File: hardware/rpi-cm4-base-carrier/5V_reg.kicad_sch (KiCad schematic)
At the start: 10 parts, among them IC5 LMR51450FNDRRR

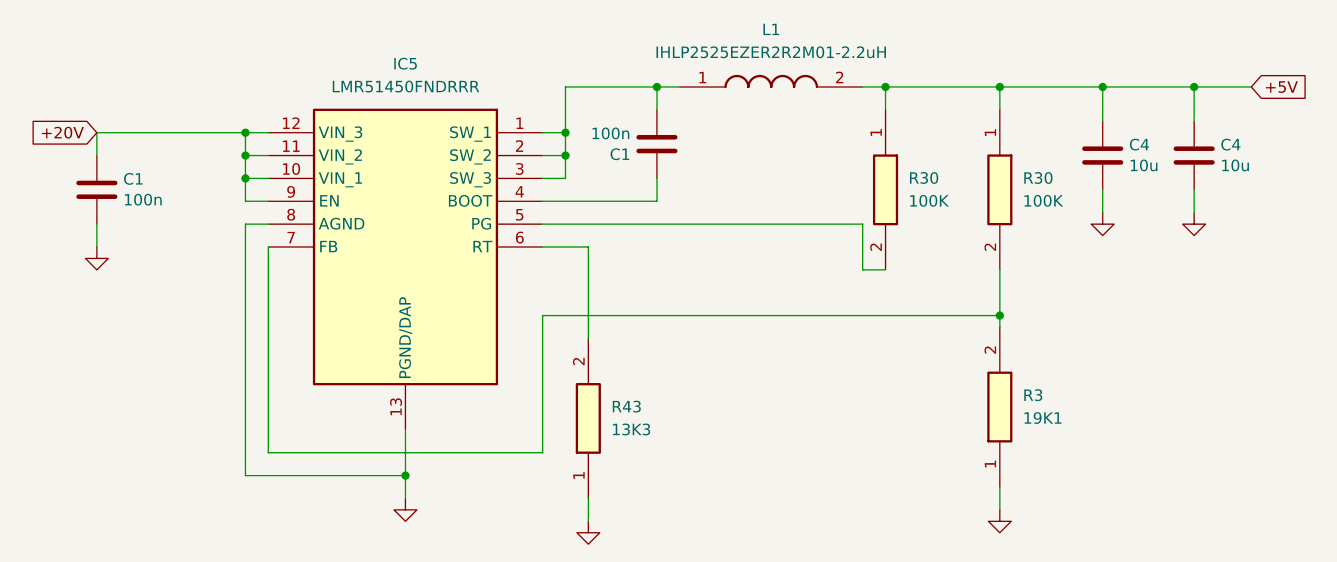
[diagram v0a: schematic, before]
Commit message: convert IC refs to U refs and re-annotate, add fiducials and extra via stitching to layout
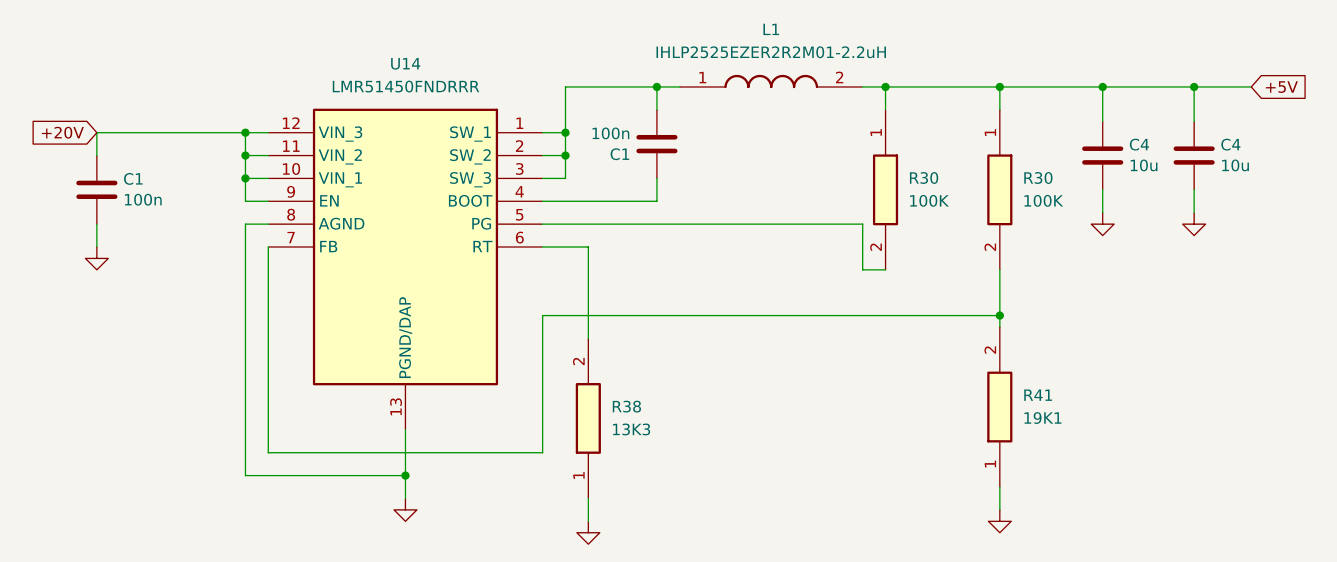
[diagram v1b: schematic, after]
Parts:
- renumbered R43 to R38, R3 to R41, IC5 to U14
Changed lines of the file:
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@@
         )
         (path "/92c58705-ecb0-498b-b561-44a3f0daad57/93ba1a48-bd63-468c-a3b4-483edb456fef/00e84fbb-dda2-4689-a88f-629944c1a860"
-          (reference "#PWR085") (unit 1)
+          (reference "#PWR088") (unit 1)
         )
       )
@@
         )
         (path "/92c58705-ecb0-498b-b561-44a3f0daad57/93ba1a48-bd63-468c-a3b4-483edb456fef/00e84fbb-dda2-4689-a88f-629944c1a860"
-          (reference "#PWR013") (unit 1)
+          (reference "#PWR086") (unit 1)
         )
       )
@@
         )
         (path "/92c58705-ecb0-498b-b561-44a3f0daad57/93ba1a48-bd63-468c-a3b4-483edb456fef/00e84fbb-dda2-4689-a88f-629944c1a860"
-          (reference "#PWR087") (unit 1)
+          (reference "#PWR091") (unit 1)
         )
       )
@@
         )
         (path "/92c58705-ecb0-498b-b561-44a3f0daad57/93ba1a48-bd63-468c-a3b4-483edb456fef/00e84fbb-dda2-4689-a88f-629944c1a860"
-          (reference "#PWR081") (unit 1)
+          (reference "#PWR089") (unit 1)
         )
       )
@@
         )
         (path "/92c58705-ecb0-498b-b561-44a3f0daad57/93ba1a48-bd63-468c-a3b4-483edb456fef/00e84fbb-dda2-4689-a88f-629944c1a860"
-          (reference "R42") (unit 1)
+          (reference "R39") (unit 1)
         )
       )
@@
         )
         (path "/92c58705-ecb0-498b-b561-44a3f0daad57/93ba1a48-bd63-468c-a3b4-483edb456fef/00e84fbb-dda2-4689-a88f-629944c1a860"
-          (reference "#PWR079") (unit 1)
+          (reference "#PWR087") (unit 1)
         )
       )
@@
   (symbol (lib_id "SamacSys_Parts:CR0402-FX-1332GLF") (at 114.3 86.36 90) (unit 1)
     (in_bom yes) (on_board yes) (dnp no) (fields_autoplaced)
-    (property "Reference" "R43" (at 116.84 76.2 90)
+    (property "Reference" "R38" (at 116.84 76.2 90)
       (effects (font (size 1.27 1.27)) (justify right))
     )
@@
       (project "rpi-cm4-base-carrier"
         (path "/92c58705-ecb0-498b-b561-44a3f0daad57/93ba1a48-bd63-468c-a3b4-483edb456fef/00e84fbb-dda2-4689-a88f-629944c1a860"
-          (reference "R43") (unit 1)
+          (reference "R38") (unit 1)
         )
       )
@@
         )
         (path "/92c58705-ecb0-498b-b561-44a3f0daad57/93ba1a48-bd63-468c-a3b4-483edb456fef/00e84fbb-dda2-4689-a88f-629944c1a860"
-          (reference "#PWR086") (unit 1)
+          (reference "#PWR090") (unit 1)
         )
       )
@@
   (symbol (lib_id "SamacSys_Parts:LMR51450FNDRRR") (at 109.22 45.72 0) (mirror y) (unit 1)
     (in_bom yes) (on_board yes) (dnp no)
-    (property "Reference" "IC5" (at 93.98 38.1 0)
+    (property "Reference" "U14" (at 93.98 38.1 0)
       (effects (font (size 1.27 1.27)))
     )
@@
       (project "rpi-cm4-base-carrier"
         (path "/92c58705-ecb0-498b-b561-44a3f0daad57/93ba1a48-bd63-468c-a3b4-483edb456fef/00e84fbb-dda2-4689-a88f-629944c1a860"
-          (reference "IC5") (unit 1)
+          (reference "U14") (unit 1)
         )
       )
@@
   (symbol (lib_id "SamacSys_Parts:CR0402-FX-1912GLF") (at 160.02 85.09 90) (unit 1)
     (in_bom yes) (on_board yes) (dnp no) (fields_autoplaced)
-    (property "Reference" "R3" (at 162.56 74.93 90)
+    (property "Reference" "R41" (at 162.56 74.93 90)
       (effects (font (size 1.27 1.27)) (justify right))
     )
@@
       (project "rpi-cm4-base-carrier"
         (path "/92c58705-ecb0-498b-b561-44a3f0daad57/93ba1a48-bd63-468c-a3b4-483edb456fef/00e84fbb-dda2-4689-a88f-629944c1a860"
-          (reference "R3") (unit 1)
+          (reference "R41") (unit 1)
         )
       )
@@
         )
         (path "/92c58705-ecb0-498b-b561-44a3f0daad57/93ba1a48-bd63-468c-a3b4-483edb456fef/00e84fbb-dda2-4689-a88f-629944c1a860"
-          (reference "R1") (unit 1)
-        )
-      )
+          (reference "R40") (unit 1)
+        )
+      )

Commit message: design files exported ready for manufacture, LCSC part numbers added throughout the library
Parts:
- C1: LCSC Part # (none) -> C152724; LCSC Part Number (none) -> C152724
- C4: LCSC Part # (none) -> C326595; LCSC Part Number (none) -> C326595
- L1: LCSC Part # (none) -> C845037; LCSC Part Number (none) -> C845037
- R30: LCSC Part # (none) -> C131362; LCSC Part Number (none) -> C131362
- R38: LCSC Part # (none) -> C274352; LCSC Part Number (none) -> C274352
- R41: LCSC Part # (none) -> C850847; LCSC Part Number (none) -> C850847
- U14: LCSC Part # (none) -> C6890985; LCSC Part Number (none) -> C6890985
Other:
- title: (none) -> Raspberry Pi Compute Module 4 Control Node
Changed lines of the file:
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@@
 (kicad_sch (version 20230121) (generator eeschema)
   (paper "A4")
+  (title_block
+    (title "Raspberry Pi Compute Module 4 Control Node")
+    (date "2024-02-04")
+    (comment 2 "creativecommons.org/licenses/by-sa/4.0/")
+    (comment 3 "License: CC BY-SA 4.0")
+    (comment 4 "Author: Sam Earnshaw")
+  )
   (junction (at 111.76 45.72) (diameter 0) (color 0 0 0 0)
   )
@@
       (effects (font (size 1.27 1.27)) hide)
     )
+    (property "LCSC Part Number" "C152724" (at 59.69 52.07 0)
+      (effects (font (size 1.27 1.27)) hide)
+    )
+    (property "LCSC Part #" "C152724" (at 59.69 52.07 0)
+      (effects (font (size 1.27 1.27)) hide)
+    )
     (pin "1")
     (pin "2")
@@
       (effects (font (size 1.27 1.27)) hide)
     )
+    (property "LCSC Part Number" "C152724" (at 121.92 46.99 0)
+      (effects (font (size 1.27 1.27)) hide)
+    )
+    (property "LCSC Part #" "C152724" (at 121.92 46.99 0)
+      (effects (font (size 1.27 1.27)) hide)
+    )
     (pin "1")
     (pin "2")
@@
     (property "Manufacturer_Part_Number" "CR0402-FX-1003GLF" (at -648.87 57.15 0)
       (effects (font (size 1.27 1.27)) (justify left top) hide)
+    )
+    (property "LCSC Part Number" "C131362" (at 147.32 43.18 0)
+      (effects (font (size 1.27 1.27)) hide)
+    )
+    (property "LCSC Part #" "C131362" (at 147.32 43.18 0)
+      (effects (font (size 1.27 1.27)) hide)
     )
     (pin "2")
@@
       (effects (font (size 1.27 1.27)) (justify left top) hide)
     )
+    (property "LCSC Part Number" "C845037" (at 124.46 40.64 0)
+      (effects (font (size 1.27 1.27)) hide)
+    )
+    (property "LCSC Part #" "C845037" (at 124.46 40.64 0)
+      (effects (font (size 1.27 1.27)) hide)
+    )
     (pin "2")
     (pin "1")
@@
     )
     (property "Field8" "111893011" (at 181.61 48.26 0)
+      (effects (font (size 1.27 1.27)) hide)
+    )
+    (property "LCSC Part Number" "C326595" (at 181.61 48.26 0)
+      (effects (font (size 1.27 1.27)) hide)
+    )
+    (property "LCSC Part #" "C326595" (at 181.61 48.26 0)
       (effects (font (size 1.27 1.27)) hide)
     )
@@
       (effects (font (size 1.27 1.27)) (justify left top) hide)
     )
+    (property "LCSC Part Number" "C274352" (at 114.3 86.36 0)
+      (effects (font (size 1.27 1.27)) hide)
+    )
+    (property "LCSC Part #" "C274352" (at 114.3 86.36 0)
+      (effects (font (size 1.27 1.27)) hide)
+    )
     (pin "1")
     (pin "2")
@@
     )
     (property "Field8" "111893011" (at 171.45 48.26 0)
+      (effects (font (size 1.27 1.27)) hide)
+    )
+    (property "LCSC Part Number" "C326595" (at 171.45 48.26 0)
+      (effects (font (size 1.27 1.27)) hide)
+    )
+    (property "LCSC Part #" "C326595" (at 171.45 48.26 0)
       (effects (font (size 1.27 1.27)) hide)
     )
@@
     (property "Manufacturer_Part_Number" "LMR51450FNDRRR" (at 82.55 840.64 0)
       (effects (font (size 1.27 1.27)) (justify left top) hide)
+    )
+    (property "LCSC Part Number" "C6890985" (at 109.22 45.72 0)
+      (effects (font (size 1.27 1.27)) hide)
+    )
+    (property "LCSC Part #" "C6890985" (at 109.22 45.72 0)
+      (effects (font (size 1.27 1.27)) hide)
     )
     (pin "13")
@@
       (effects (font (size 1.27 1.27)) (justify left top) hide)
     )
+    (property "LCSC Part Number" "C850847" (at 160.02 85.09 0)
+      (effects (font (size 1.27 1.27)) hide)
+    )
+    (property "LCSC Part #" "C850847" (at 160.02 85.09 0)
+      (effects (font (size 1.27 1.27)) hide)
+    )
     (pin "2")
     (pin "1")
@@
       (effects (font (size 1.27 1.27)) (justify left top) hide)
     )
+    (property "LCSC Part Number" "C131362" (at 160.02 43.18 0)
+      (effects (font (size 1.27 1.27)) hide)
+    )
+    (property "LCSC Part #" "C131362" (at 160.02 43.18 0)
+      (effects (font (size 1.27 1.27)) hide)
+    )
     (pin "2")
